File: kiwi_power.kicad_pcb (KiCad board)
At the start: 2 copper layers, 100 x 92 mm, 59 parts, among them J1 PSU, J10 Power_output, J2 Battery, J3 emergency_stop, J4 Power_always, J5 Power_stop, J6 Power_output, J7 Power_output, J8 Power_output, J9 Power_output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

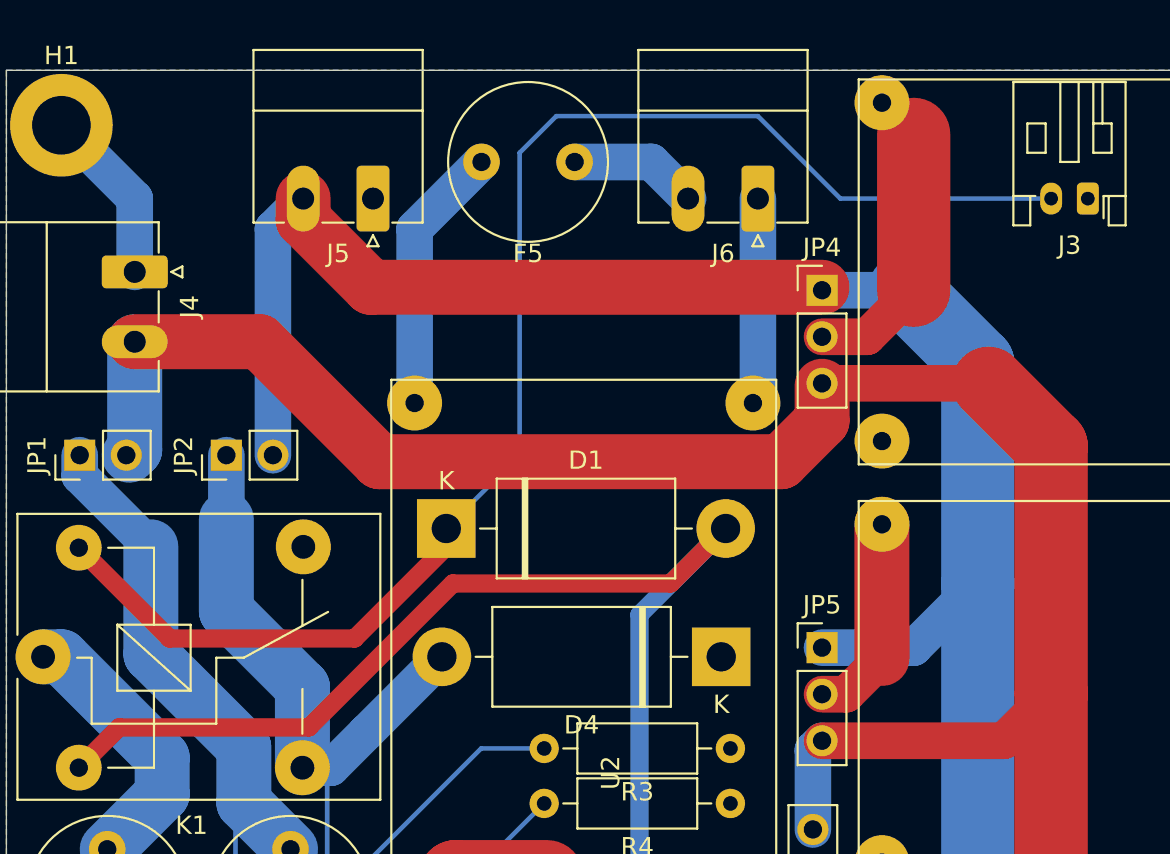
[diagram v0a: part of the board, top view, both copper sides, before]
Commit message: fixing wrong diode symbol for simulation only
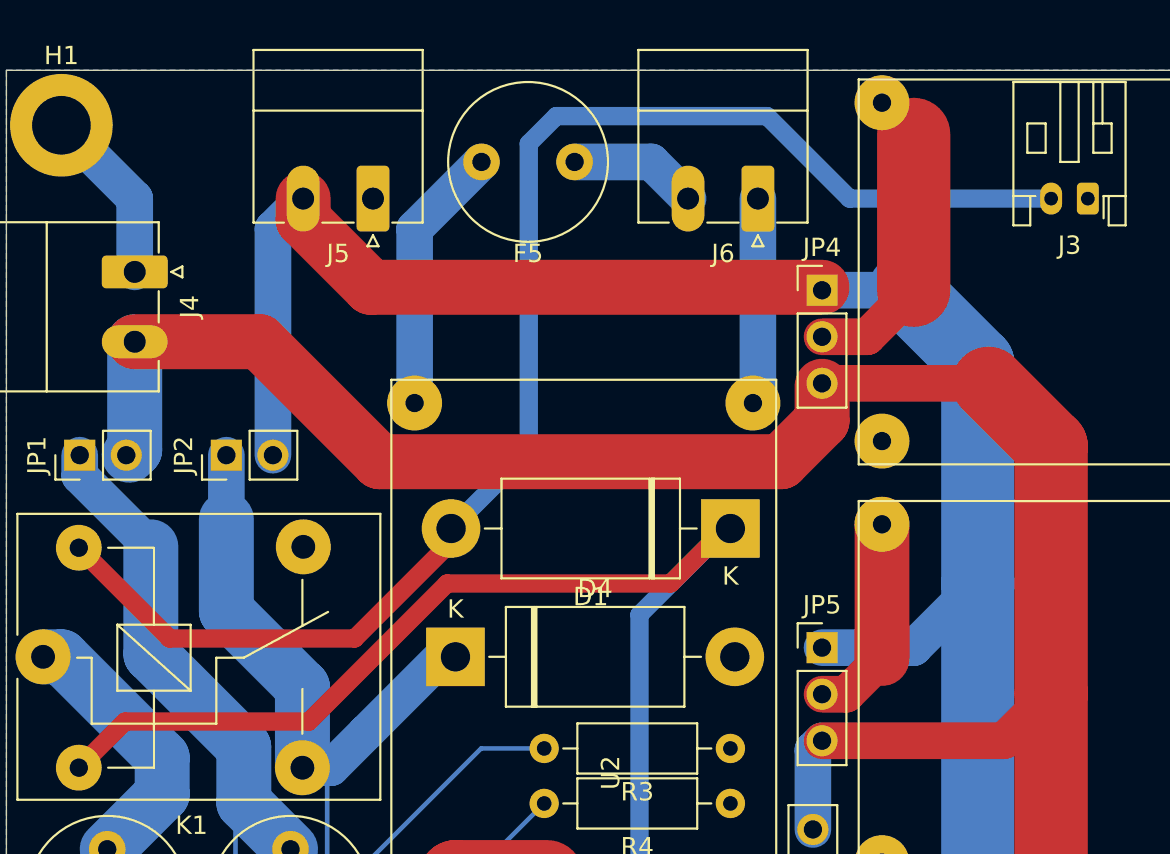
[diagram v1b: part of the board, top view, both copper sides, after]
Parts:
- D1, D4: value DIODE -> D_ALT
- moved D1 15.5 mm to (219.5, 45.0), turned to 180 degrees
- moved D4 14.5 mm to (204.5, 52.0), turned to 0 degrees
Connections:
- D1 pad 1: /power_input/emergency_stop -> Net-(C2-Pad1)
- D1 pad 2: Net-(C2-Pad1) -> /power_input/emergency_stop
- D4 pad 1: GND -> /power_input/V_power_stop
- D4 pad 2: /power_input/V_power_stop -> GND

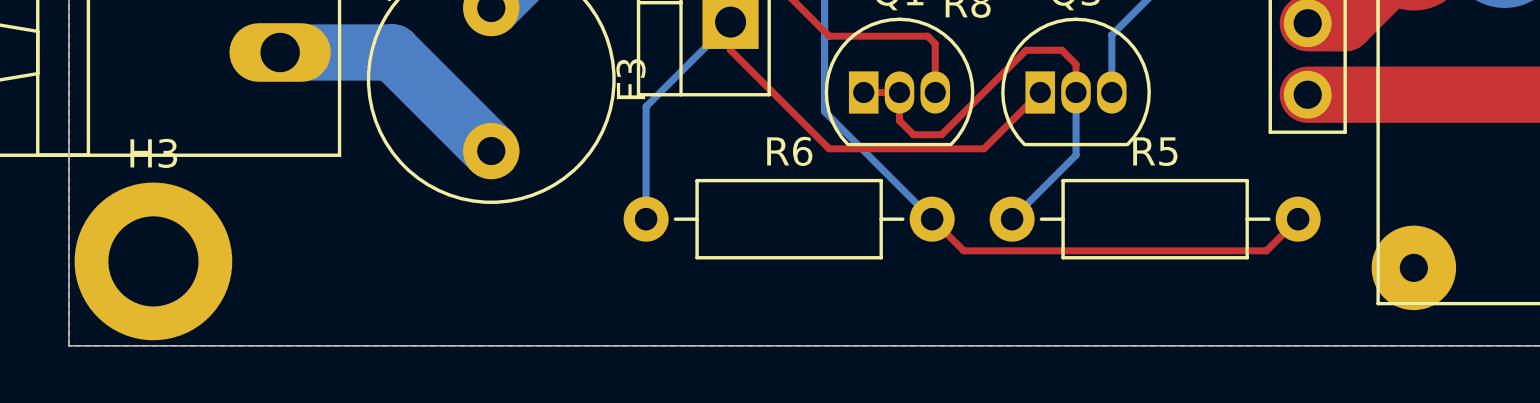
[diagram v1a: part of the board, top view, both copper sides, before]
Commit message: added link and logo
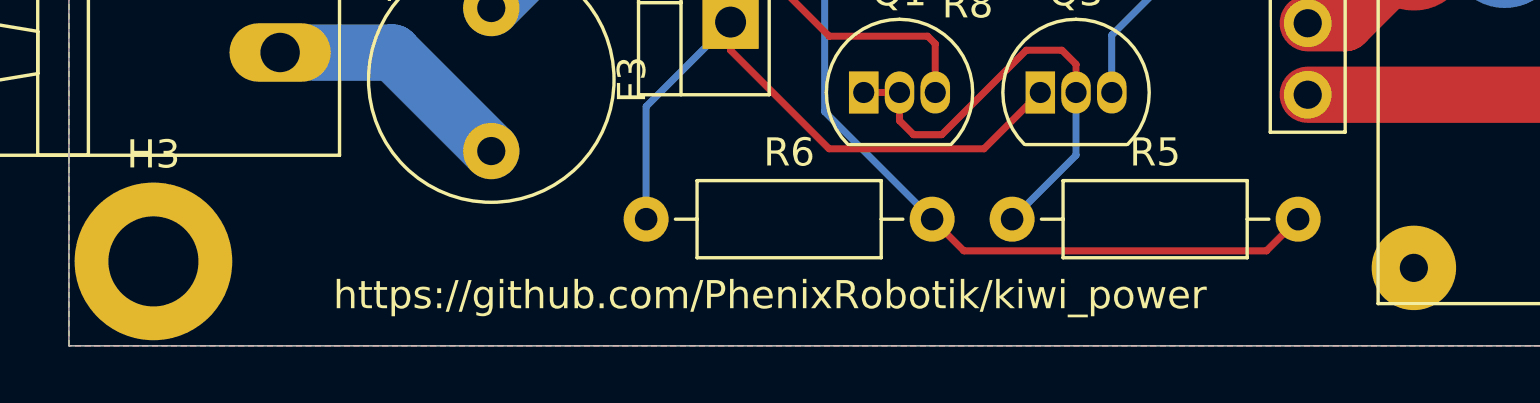
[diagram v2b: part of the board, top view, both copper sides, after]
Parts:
- added G***: LOGO, kiwi_power:pcb_logo, B.Cu at (227.5, 72.2)
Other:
- board text added: "https://github.com/PhenixRobotik/kiwi_power"

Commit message: version 2
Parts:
- removed G***: LOGO, kiwi_power:pcb_logo
- removed Q1, Q3, Q4, Q6: BC327, Package_TO_SOT_THT:TO-92_Inline
- removed Q2, Q5: IRF9540N, Package_TO_SOT_THT:TO-220-3_Vertical
- removed R5, R6, R7, R8: R, Resistor_THT:R_Axial_DIN0207_L6.3mm_D2.5mm_P10.16mm_Horizontal
- added D5: C3D16060D, Package_TO_SOT_THT:TO-220-3_Vertical, F.Cu at (214.6, 103.6)
- added JP8: Jumper_NO_Small, Connector_PinHeader_2.54mm:PinHeader_1x02_P2.54mm_Vertical, F.Cu at (201.0, 35.5)
- added JP9: Jumper_NO_Small, Connector_PinHeader_2.54mm:PinHeader_1x02_P2.54mm_Vertical, F.Cu at (207.5, 35.5)
- added RV3: Varistor, Varistor:RV_Disc_D7mm_W4mm_P5mm, F.Cu at (201.4, 92.2)
- D1, D4: footprint Diode_THT:D_DO-201AD_P15.24mm_Horizontal -> Diode_THT:D_DO-35_SOD27_P10.16mm_Horizontal
- moved J3 48.5 mm to (190.5, 26.7)
- moved D1 29.2 mm to (194.5, 60.0)
- moved R2 24.1 mm to (218.0, 99.0)
- moved R1 23.9 mm to (205.0, 95.5)
- moved D4 22.6 mm to (195.0, 31.5), turned to 180 degrees
- moved JP1 19.5 mm to (201.0, 31.5)
- moved R3 18.5 mm to (213.5, 74.5)
- moved JP2 15.6 mm to (207.5, 39.5)
- moved J4 13.6 mm to (200.0, 27.0), turned to 180 degrees
- moved R4 12.5 mm to (213.5, 71.0)
- moved C1 11.0 mm to (221.0, 95.0)
- moved J5 10.5 mm to (210.5, 27.0)
- moved F5 10.0 mm to (217.0, 33.0), turned to 270 degrees
- moved U1 8.38 mm to (209.5, 92.0)
- moved K1 8.31 mm to (190.0, 54.2), turned to 90 degrees
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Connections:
- net Net-(F4-Pad1) renamed /power_input/sheet61577D25/Vout+
- C1 pad 1: /power_input/input_bloc/Vout+ -> Net-(C1-Pad1)
- F1 pad 2: /power_input/input_bloc/Vout+ -> Net-(C1-Pad1)
- F2 pad 2: /power_input/input_bloc/Vout+ -> Net-(C1-Pad1)
- F3 pad 1: Net-(F3-Pad1) -> /power_input/input_bloc/Vout+
- RV1 pad 1: Net-(F3-Pad1) -> /power_input/input_bloc/Vout+
- U1 pad 3: /power_input/input_bloc/Vout+ -> Net-(C1-Pad1)
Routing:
- net GND: track 107.0 -> 11.3 mm
- net Net-(C1-Pad1): track 0.00 -> 77.5 mm
- net /power_input/input_bloc/Vout+: track 89.7 -> 38.0 mm
- net /power_input/emergency_stop: track 79.4 -> 35.3 mm
- net Net-(Q2-Pad1): track 22.5 -> 0.00 mm
- net Net-(Q5-Pad1): track 22.2 -> 0.00 mm
- net Net-(D2-Pad1): track 28.9 -> 7.34 mm
- net Net-(F3-Pad1): track 21.4 -> 0.00 mm
- net /power_input/V_power_stop: track 52.2 -> 69.4 mm
- net Net-(Q1-Pad1): track 16.6 -> 0.00 mm
- net Net-(D3-Pad1): track 40.4 -> 24.5 mm
- net Net-(Q4-Pad1): track 15.9 -> 0.00 mm
- net Net-(C2-Pad1): track 98.1 -> 84.7 mm
- net /regulators/V_in_stop: track 150.1 -> 138.9 mm
- net /power_input/V_power_always: track 44.6 -> 49.7 mm
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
